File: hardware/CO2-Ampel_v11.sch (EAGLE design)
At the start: 74 parts, among them IC1 ATSAMD21G18A-MU, IC2 VREG-AP2111H-3V3, IC3 SCD30, IC4 ATECC608A-MAHDA, IC5 ATWINC1500-MR210PB, J1 USB-C-S, J2 SWD-2X5-SMD, J3 SWD-1X5-SMDNC, J4 JST4-SM04B-SRSS-TB, J5 JST4-SM04B-SRSS-TB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

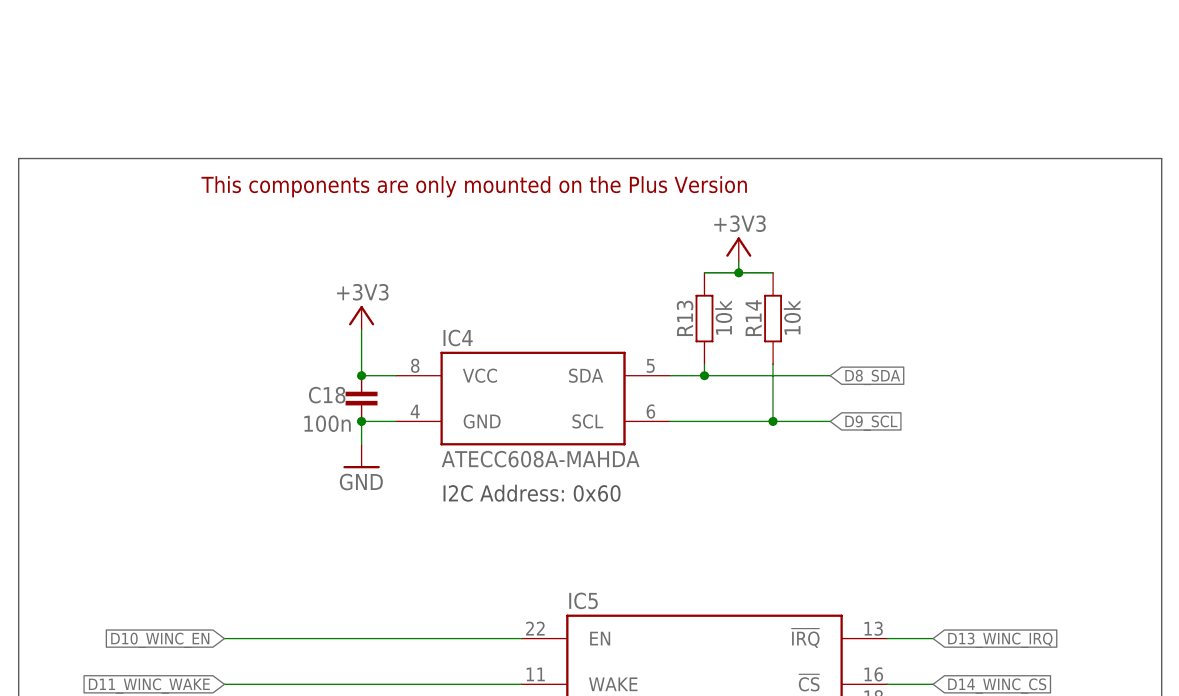
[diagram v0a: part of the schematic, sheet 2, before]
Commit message: updated schematics
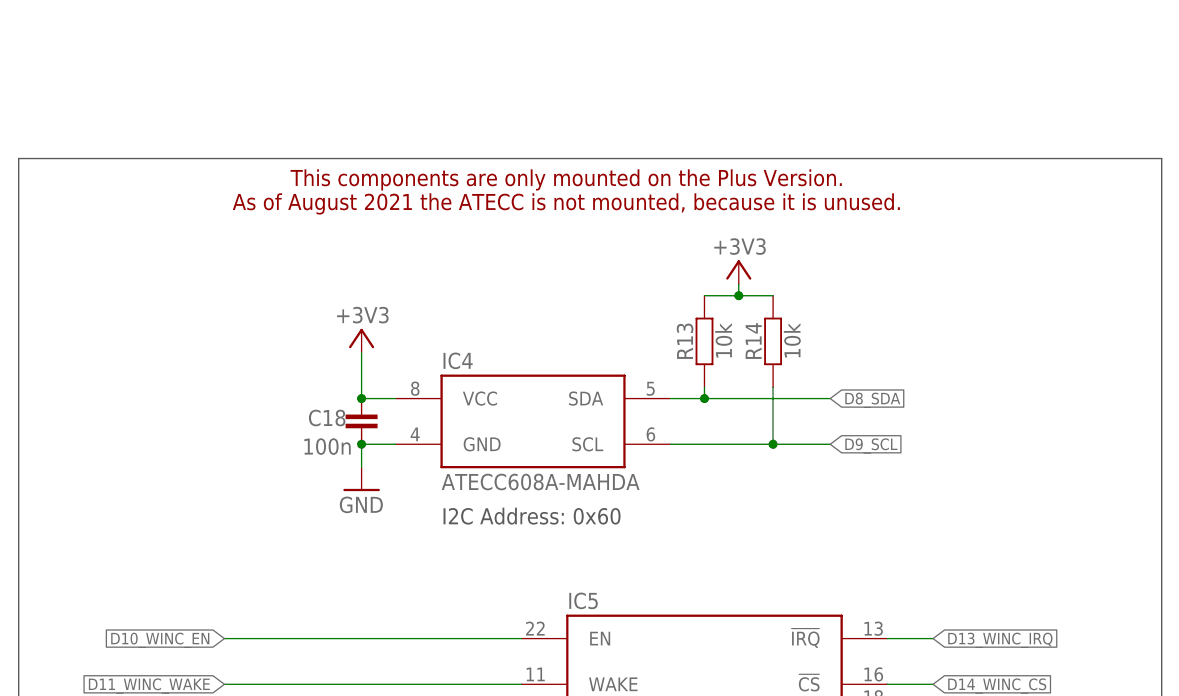
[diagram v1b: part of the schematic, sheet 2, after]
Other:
- note added: "This components are only mounted on the Plus Version. As of August 2021 the ATECC is not mounted, because it is unused."
- note removed: "This components are only mounted on the Plus Version"
- moved on the sheet: C18, IC4, R13, R14
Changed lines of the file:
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@@
 <sheet>
 <plain>
-<text x="52.07" y="73.66" size="1.778" layer="97">I2C Address: 0x60</text>
+<text x="52.07" y="71.12" size="1.778" layer="97">I2C Address: 0x60</text>
 <text x="162.56" y="22.86" size="1.27" layer="95" align="top-left">Released under the Creative Commons Attribution Share-Alike
 License. http://creativecommons.org/licenses/by-sa/4.0/
 Designed by Watterott electronic</text>
-<text x="25.4" y="107.95" size="1.778" layer="94" font="vector" ratio="13">This components are only mounted on the Plus Version</text>
+<text x="66.04" y="110.49" size="1.778" layer="94" font="vector" ratio="13" align="top-center">This components are only mounted on the Plus Version.
+As of August 2021 the ATECC is not mounted, because it is unused.</text>
 <wire x1="5.08" y1="5.08" x2="132.08" y2="5.08" width="0.1524" layer="97"/>
 <wire x1="132.08" y1="5.08" x2="132.08" y2="111.76" width="0.1524" layer="97"/>
@@
 <attribute name="VALUE" x="138.43" y="137.16" size="1.778" layer="96" align="top-center"/>
 </instance>
-<instance part="+3V315" gate="G$1" x="43.18" y="95.25" smashed="yes">
-<attribute name="VALUE" x="46.355" y="97.79" size="1.778" layer="96" rot="R180"/>
-</instance>
-<instance part="C18" gate="C" x="43.18" y="85.09" smashed="yes" rot="R90">
-<attribute name="NAME" x="39.37" y="86.36" size="1.778" layer="95" rot="R180" align="bottom-center"/>
-<attribute name="VALUE" x="39.37" y="83.185" size="1.778" layer="96" align="top-center"/>
-</instance>
-<instance part="GND34" gate="1" x="43.18" y="77.47" smashed="yes">
-<attribute name="VALUE" x="40.64" y="74.93" size="1.778" layer="96"/>
-</instance>
-<instance part="IC4" gate="IC" x="62.23" y="85.09" smashed="yes">
-<attribute name="NAME" x="52.07" y="92.71" size="1.778" layer="95" align="top-left"/>
-<attribute name="VALUE" x="52.07" y="77.47" size="1.778" layer="95"/>
+<instance part="+3V315" gate="G$1" x="43.18" y="92.71" smashed="yes">
+<attribute name="VALUE" x="46.355" y="95.25" size="1.778" layer="96" rot="R180"/>
+</instance>
+<instance part="C18" gate="C" x="43.18" y="82.55" smashed="yes" rot="R90">
+<attribute name="NAME" x="39.37" y="83.82" size="1.778" layer="95" rot="R180" align="bottom-center"/>
+<attribute name="VALUE" x="39.37" y="80.645" size="1.778" layer="96" align="top-center"/>
+</instance>
+<instance part="GND34" gate="1" x="43.18" y="74.93" smashed="yes">
+<attribute name="VALUE" x="40.64" y="72.39" size="1.778" layer="96"/>
+</instance>
+<instance part="IC4" gate="IC" x="62.23" y="82.55" smashed="yes">
+<attribute name="NAME" x="52.07" y="90.17" size="1.778" layer="95" align="top-left"/>
+<attribute name="VALUE" x="52.07" y="74.93" size="1.778" layer="95"/>
 </instance>
 <instance part="J5" gate="J" x="203.2" y="64.77" smashed="yes">
@@
 <attribute name="VALUE" x="138.43" y="143.51" size="1.778" layer="96"/>
 </instance>
-<instance part="R13" gate="R" x="81.28" y="93.98" smashed="yes" rot="R90">
-<attribute name="NAME" x="80.01" y="93.98" size="1.778" layer="95" rot="R90" align="bottom-center"/>
-<attribute name="VALUE" x="82.55" y="93.98" size="1.778" layer="96" rot="R90" align="top-center"/>
-</instance>
-<instance part="R14" gate="R" x="88.9" y="93.98" smashed="yes" rot="R90">
-<attribute name="NAME" x="87.63" y="93.98" size="1.778" layer="95" rot="R90" align="bottom-center"/>
-<attribute name="VALUE" x="90.17" y="93.98" size="1.778" layer="96" rot="R90" align="top-center"/>
-</instance>
-<instance part="+3V1" gate="G$1" x="85.09" y="102.87" smashed="yes">
-<attribute name="VALUE" x="88.265" y="105.41" size="1.778" layer="96" rot="R180"/>
+<instance part="R13" gate="R" x="81.28" y="91.44" smashed="yes" rot="R90">
+<attribute name="NAME" x="80.01" y="91.44" size="1.778" layer="95" rot="R90" align="bottom-center"/>
+<attribute name="VALUE" x="82.55" y="91.44" size="1.778" layer="96" rot="R90" align="top-center"/>
+</instance>
+<instance part="R14" gate="R" x="88.9" y="91.44" smashed="yes" rot="R90">
+<attribute name="NAME" x="87.63" y="91.44" size="1.778" layer="95" rot="R90" align="bottom-center"/>
+<attribute name="VALUE" x="90.17" y="91.44" size="1.778" layer="96" rot="R90" align="top-center"/>
+</instance>
+<instance part="+3V1" gate="G$1" x="85.09" y="100.33" smashed="yes">
+<attribute name="VALUE" x="88.265" y="102.87" size="1.778" layer="96" rot="R180"/>
 </instance>
 <instance part="R8" gate="R" x="224.79" y="149.86" smashed="yes" rot="R90">
@@
 <segment>
 <pinref part="C18" gate="C" pin="1"/>
-<wire x1="46.99" y1="82.55" x2="43.18" y2="82.55" width="0.1524" layer="91"/>
+<wire x1="46.99" y1="80.01" x2="43.18" y2="80.01" width="0.1524" layer="91"/>
 <pinref part="GND34" gate="1" pin="GND"/>
-<wire x1="43.18" y1="82.55" x2="43.18" y2="80.01" width="0.1524" layer="91"/>
-<junction x="43.18" y="82.55"/>
+<wire x1="43.18" y1="80.01" x2="43.18" y2="77.47" width="0.1524" layer="91"/>
+<junction x="43.18" y="80.01"/>
 <pinref part="IC4" gate="IC" pin="GND"/>
 </segment>
@@
 <segment>
 <pinref part="C18" gate="C" pin="2"/>
-<wire x1="46.99" y1="87.63" x2="43.18" y2="87.63" width="0.1524" layer="91"/>
+<wire x1="46.99" y1="85.09" x2="43.18" y2="85.09" width="0.1524" layer="91"/>
 <pinref part="+3V315" gate="G$1" pin="+3V3"/>
-<wire x1="43.18" y1="87.63" x2="43.18" y2="92.71" width="0.1524" layer="91"/>
-<junction x="43.18" y="87.63"/>
+<wire x1="43.18" y1="85.09" x2="43.18" y2="90.17" width="0.1524" layer="91"/>
+<junction x="43.18" y="85.09"/>
 <pinref part="IC4" gate="IC" pin="VCC"/>
 </segment>
@@
 <pinref part="R13" gate="R" pin="2"/>
 <pinref part="R14" gate="R" pin="2"/>
-<wire x1="81.28" y1="99.06" x2="85.09" y2="99.06" width="0.1524" layer="91"/>
+<wire x1="81.28" y1="96.52" x2="85.09" y2="96.52" width="0.1524" layer="91"/>
 <pinref part="+3V1" gate="G$1" pin="+3V3"/>
-<wire x1="85.09" y1="99.06" x2="88.9" y2="99.06" width="0.1524" layer="91"/>
-<wire x1="85.09" y1="100.33" x2="85.09" y2="99.06" width="0.1524" layer="91"/>
-<junction x="85.09" y="99.06"/>
+<wire x1="85.09" y1="96.52" x2="88.9" y2="96.52" width="0.1524" layer="91"/>
+<wire x1="85.09" y1="97.79" x2="85.09" y2="96.52" width="0.1524" layer="91"/>
+<junction x="85.09" y="96.52"/>
 </segment>
 <segment>
@@
 <net name="D8_SDA" class="0">
 <segment>
-<wire x1="77.47" y1="87.63" x2="81.28" y2="87.63" width="0.1524" layer="91"/>
-<label x="95.25" y="87.63" size="1.27" layer="95" xref="yes"/>
+<wire x1="77.47" y1="85.09" x2="81.28" y2="85.09" width="0.1524" layer="91"/>
+<label x="95.25" y="85.09" size="1.27" layer="95" xref="yes"/>
 <pinref part="IC4" gate="IC" pin="SDA"/>
 <pinref part="R13" gate="R" pin="1"/>
-<wire x1="81.28" y1="87.63" x2="95.25" y2="87.63" width="0.1524" layer="91"/>
-<wire x1="81.28" y1="87.63" x2="81.28" y2="88.9" width="0.1524" layer="91"/>
-<junction x="81.28" y="87.63"/>
+<wire x1="81.28" y1="85.09" x2="95.25" y2="85.09" width="0.1524" layer="91"/>
+<wire x1="81.28" y1="85.09" x2="81.28" y2="86.36" width="0.1524" layer="91"/>
+<junction x="81.28" y="85.09"/>
 </segment>
 </net>
 <net name="D9_SCL" class="0">
 <segment>
-<wire x1="77.47" y1="82.55" x2="88.9" y2="82.55" width="0.1524" layer="91"/>
-<label x="95.25" y="82.55" size="1.27" layer="95" xref="yes"/>
+<wire x1="77.47" y1="80.01" x2="88.9" y2="80.01" width="0.1524" layer="91"/>
+<label x="95.25" y="80.01" size="1.27" layer="95" xref="yes"/>
 <pinref part="IC4" gate="IC" pin="SCL"/>
 <pinref part="R14" gate="R" pin="1"/>
-<wire x1="88.9" y1="82.55" x2="95.25" y2="82.55" width="0.1524" layer="91"/>
-<wire x1="88.9" y1="82.55" x2="88.9" y2="88.9" width="0.1524" layer="91"/>
-<junction x="88.9" y="82.55"/>
-</segment>
-</net>
+<wire x1="88.9" y1="80.01" x2="95.25" y2="80.01" width="0.1524" layer="91"/>
+<wire x1="88.9" y1="80.01" x2="88.9" y2="86.36" width="0.1524" layer="91"/>
+<junction x="88.9" y="80.01"/>
+</segment>
+</net>
